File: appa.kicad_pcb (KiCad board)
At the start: 2 copper layers, 227.8 x 75.4 mm, 121 parts, among them J1 USB_B, J2 USB, J3 Columns, J4 Rows, J5 I2C, J6 ICSP, SW1 SW_DIP_x01, SW10 SW_DIP_x01, SW11 SW_DIP_x01, SW12 SW_DIP_x01, SW13 SW_DIP_x01, SW14 SW_DIP_x01, SW15 SW_DIP_x01, SW16 SW_DIP_x01, SW17 SW_DIP_x01, SW18 SW_DIP_x01, SW19 SW_DIP_x01, SW2 SW_DIP_x01, SW20 SW_DIP_x01, SW21 SW_DIP_x01, SW22 SW_DIP_x01, SW23 SW_DIP_x01, SW24 SW_DIP_x01, SW25 SW_DIP_x01, SW26 SW_DIP_x01, SW27 SW_DIP_x01, SW28 SW_DIP_x01, SW29 SW_DIP_x01, SW3 SW_DIP_x01, SW30 SW_DIP_x01, SW31 SW_DIP_x01, SW32 SW_DIP_x01, SW33 SW_DIP_x01, SW34 SW_DIP_x01, SW35 SW_DIP_x01, SW36 SW_DIP_x01, SW37 SW_DIP_x01, SW38 SW_DIP_x01, SW39 SW_DIP_x01, SW4 SW_DIP_x01, SW40 SW_DIP_x01, SW41 SW_DIP_x01, SW42 SW_DIP_x01, SW43 SW_DIP_x01, SW44 SW_DIP_x01, SW45 SW_DIP_x01, SW46 SW_DIP_x01, SW47 SW_DIP_x01, SW48 SW_DIP_x01, SW49 RESET, SW5 SW_DIP_x01, SW50 BOOT, SW6 SW_DIP_x01, SW7 SW_DIP_x01, SW8 SW_DIP_x01, SW9 SW_DIP_x01, U1 ARDUINO_PRO_MINI, U2 ATmega328-P, Y1 16MHz

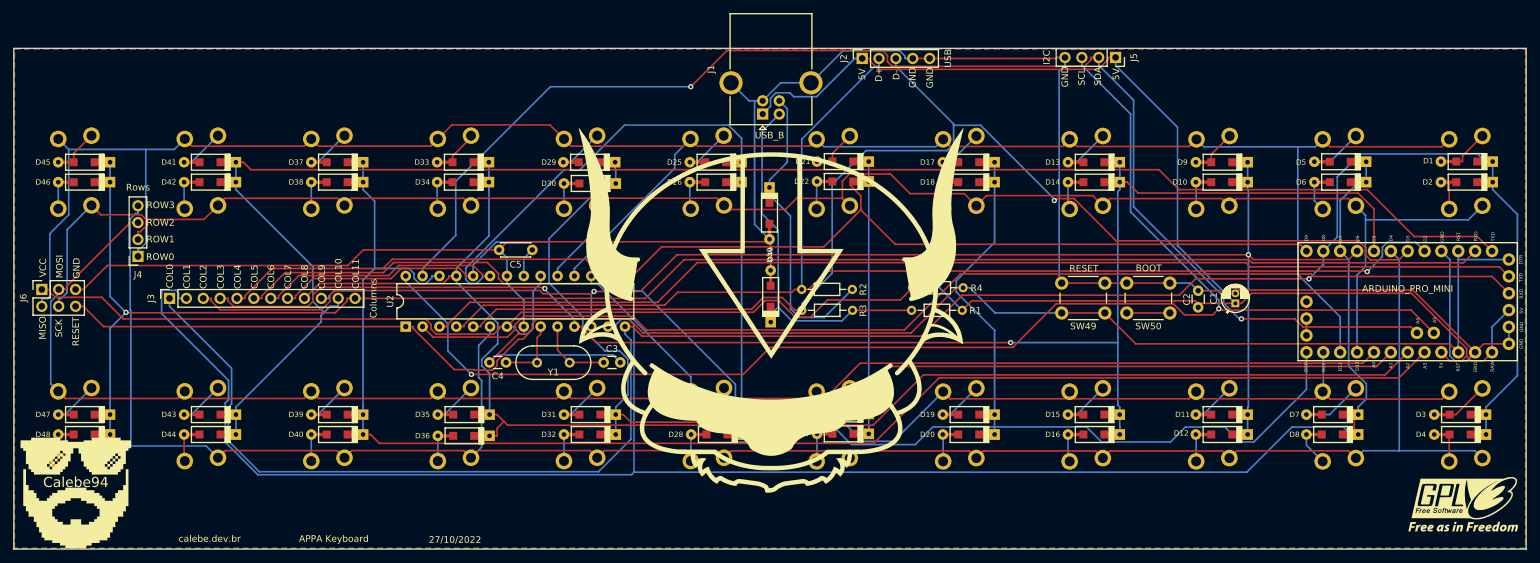
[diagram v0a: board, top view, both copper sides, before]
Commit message: Fixed unwired pins
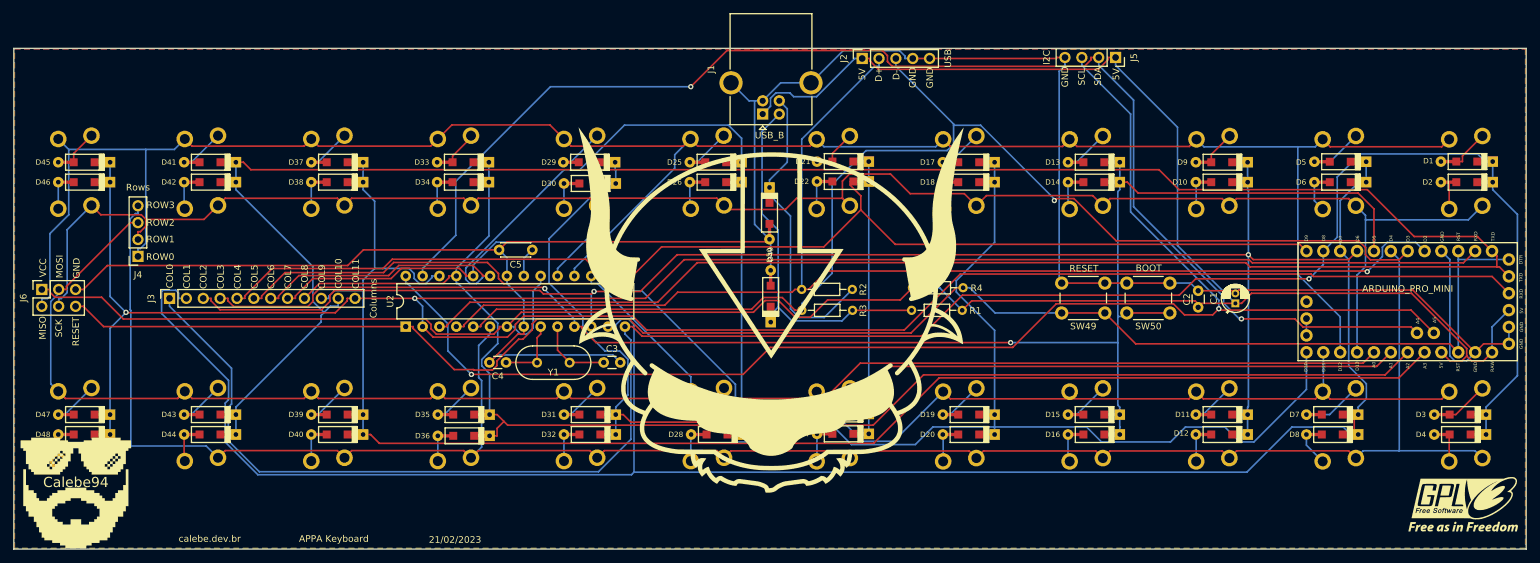
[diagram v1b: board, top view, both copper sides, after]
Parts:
- C1: value C -> C_Polarized
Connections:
- D13 pad 1: COL_3 -> BOOT
- D14 pad 1: COL_3 -> BOOT
- D15 pad 1: COL_3 -> BOOT
- D16 pad 1: COL_3 -> BOOT
- J3 pad 4: COL_3 -> BOOT
- U1 pad JP7_5: COL_3 -> BOOT
- U2 pad 11: COL_3 -> BOOT
- U2 pad 2: RXD -> COL_11
- U2 pad 3: TXD -> COL_10
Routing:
- net BOOT: track 6.50 -> 246.9 mm, vias 0 -> 2
- net COL_3: track 238.9 -> 0.00 mm, vias 2 -> 0
- net COL_11: track 259.9 -> 436.2 mm, vias 1 -> 2
- net RXD: track 171.5 -> 0.00 mm
- net COL_10: track 259.7 -> 428.4 mm
- net TXD: track 166.0 -> 0.00 mm
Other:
- board text added: "21/02/2023"
- board text removed: "27/10/2022"
